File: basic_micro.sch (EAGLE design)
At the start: 33 parts, among them IC1 PICAXE-08M2-DIL, IC2 7805, IC4 4026N, IC6 74HC08N, IC7 74HC04N, J1 POWER_JACKPTH, J2 AUDIO-JACK2PTH

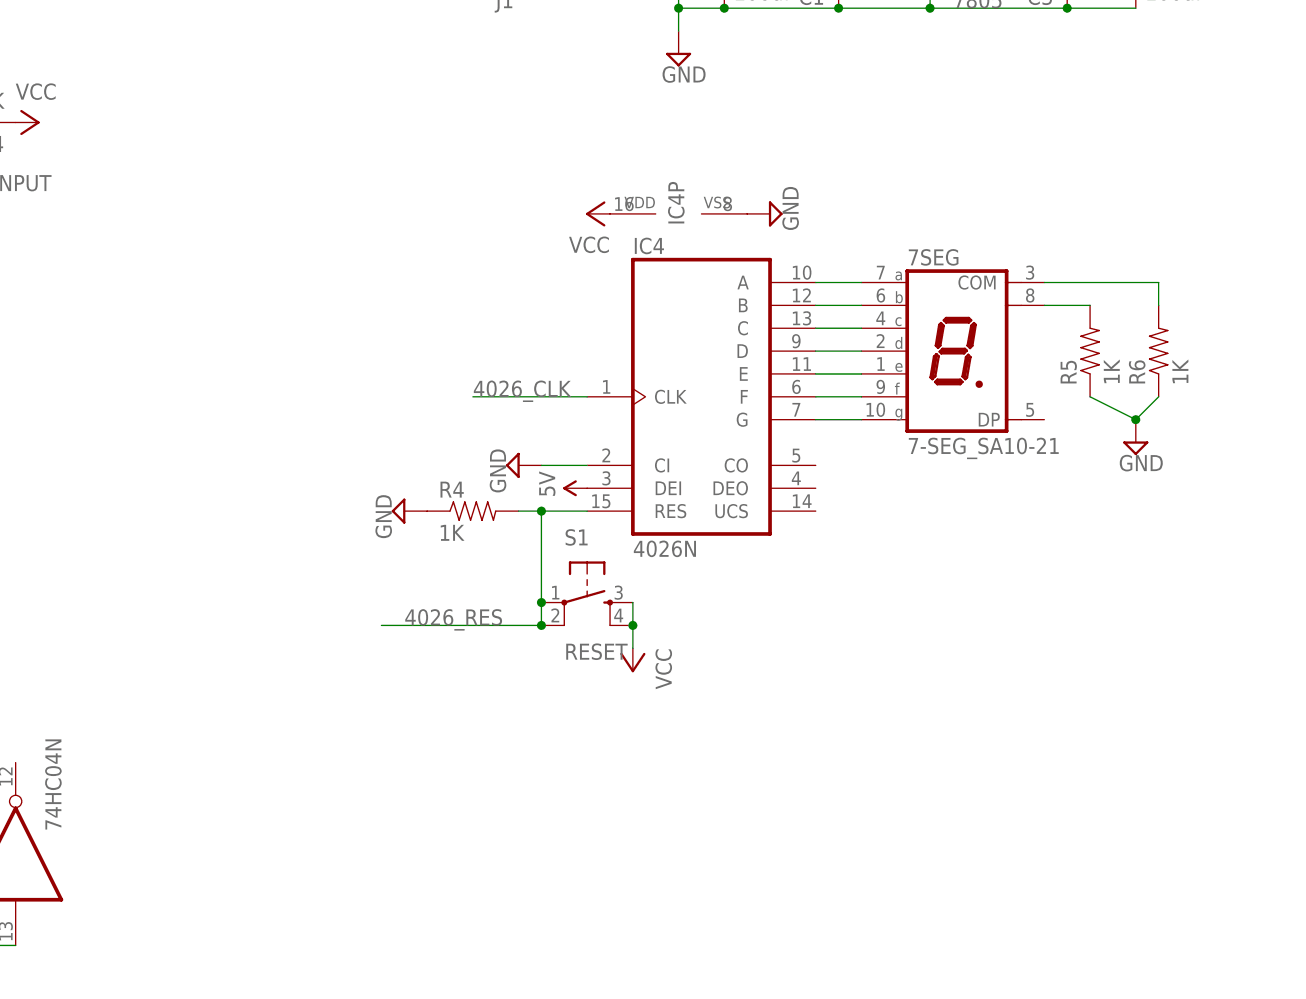
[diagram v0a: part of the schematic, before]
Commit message: Added UDN2981 between 4026 & 7SEG display
This avoids sourcing too much current from the 4026
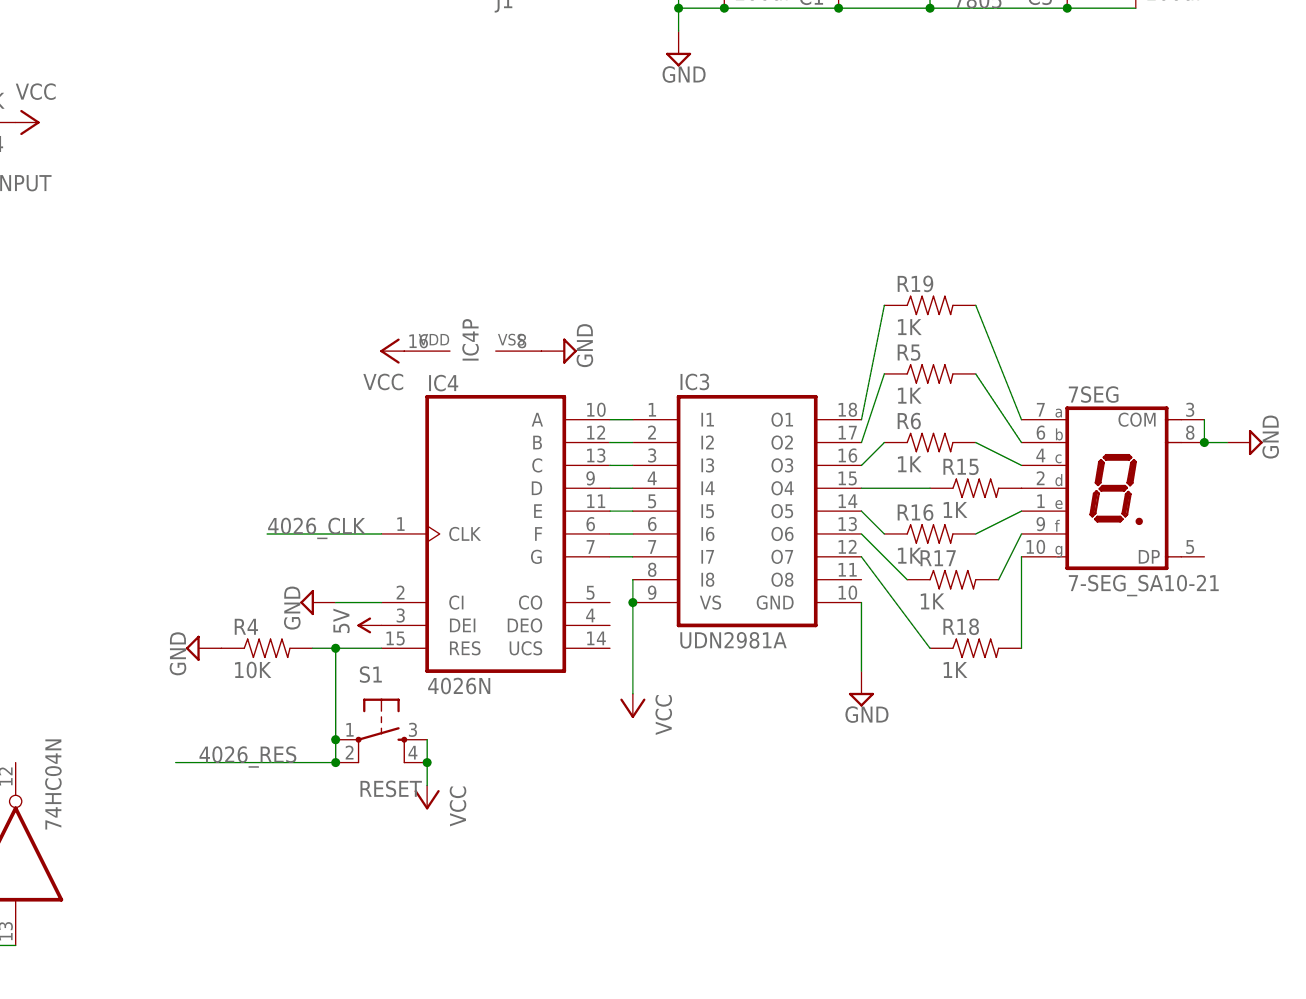
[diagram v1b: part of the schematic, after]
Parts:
- added IC3: UDN2981A, uln-udn:UDN2981A
- added R15, R16, R17, R18, R19: 1K, SparkFun-Passives:RESISTORPTH-1/4W
- R4: value 1K -> 10K
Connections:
- new net N$11: IC3.I3, IC4A.C
- new net N$12: IC3.I4, IC4A.D
- new net N$29: IC3.O7, R18.1
- new net N$30: 7SEG.A, R19.2
- new net N$31: 7SEG.B, R5.2
- new net N$32: 7SEG.C, R6.2
- new net N$33: 7SEG.D, R15.2
- new net N$34: 7SEG.E, R16.2
- new net N$35: 7SEG.F, R17.2
- new net N$36: 7SEG.G, R18.2
- new net N$5: IC3.I1, IC4A.A
- new net N$7: IC3.I2, IC4A.B
- net GND: now also 7SEG.COM@1, 7SEG.COM@2, IC3.GND; no longer R5.1, R6.1
- net N$13: now also IC3.I5, IC4A.E; no longer 7SEG.F, IC4A.F
- net N$14: now also IC3.I6, IC4A.F; no longer 7SEG.D, IC4A.D
- net N$15: now also IC3.I7, IC4A.G; no longer 7SEG.B, IC4A.B
- net N$16: now also IC3.O3, R6.1; no longer 7SEG.A, IC4A.A
- net N$17: now also IC3.O4, R15.1; no longer 7SEG.C, IC4A.C
- net N$18: now also IC3.O5, R16.1; no longer 7SEG.E, IC4A.E
- net N$19: now also IC3.O6, R17.1; no longer 7SEG.G, IC4A.G
- net N$2: now also IC3.O1, R19.1; no longer 7SEG.COM@1, R6.2
- net N$4: now also IC3.O2, R5.1; no longer 7SEG.COM@2, R5.2
- net VCC: now also IC3.I8, IC3.VS
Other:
- moved on the sheet: 7SEG, IC4, IC4P, R4, R5, R6, S1
